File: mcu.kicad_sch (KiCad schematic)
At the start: 29 parts, among them J2 Conn_01x10, J3 Conn_01x10, J4 Conn_02x05_Odd_Even, U7 STM32F407VGTx, U8 STM809SWX6F, Y1 8MHz

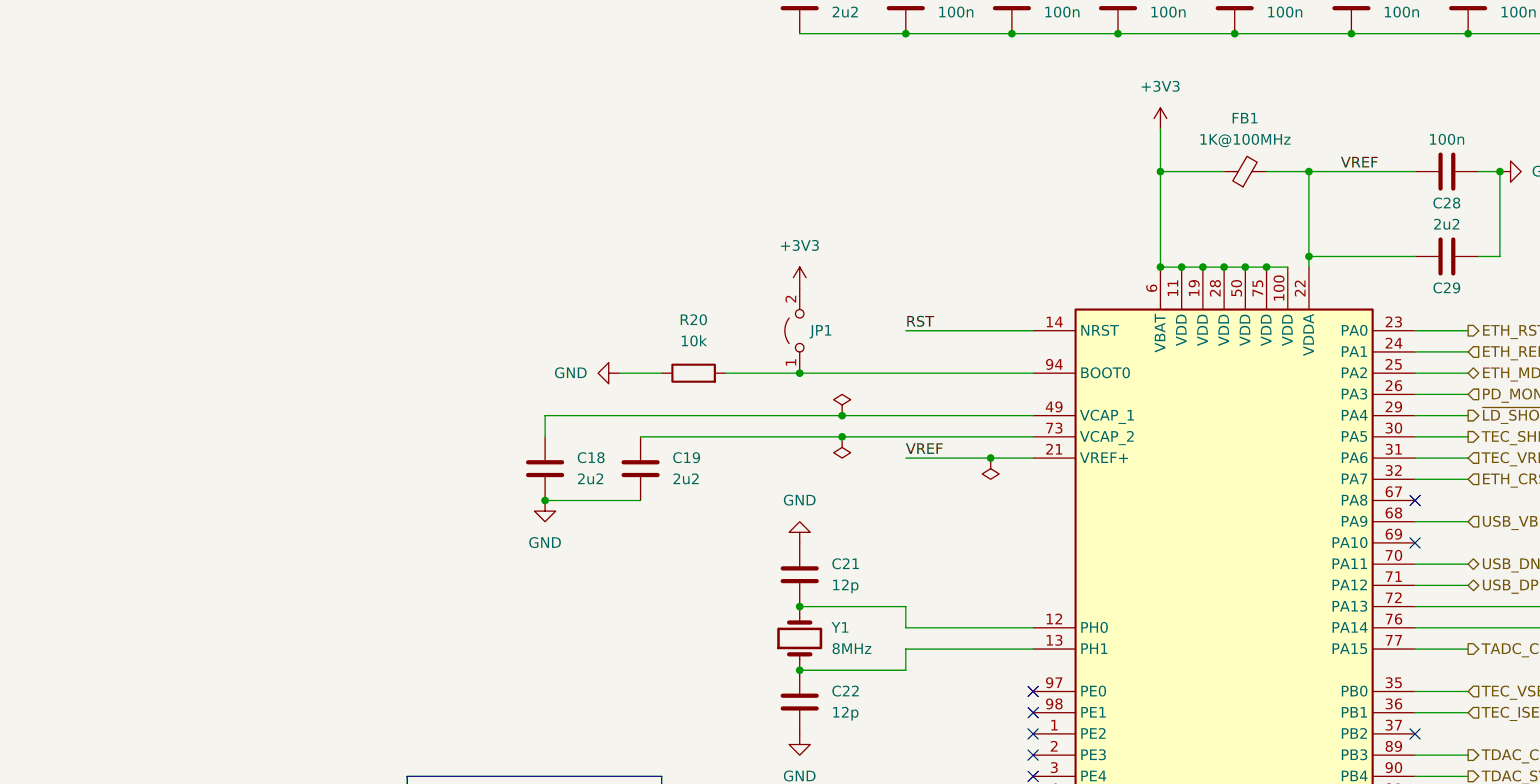
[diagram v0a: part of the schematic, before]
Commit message: sch: Add REF3033 for MCU ADC VREF
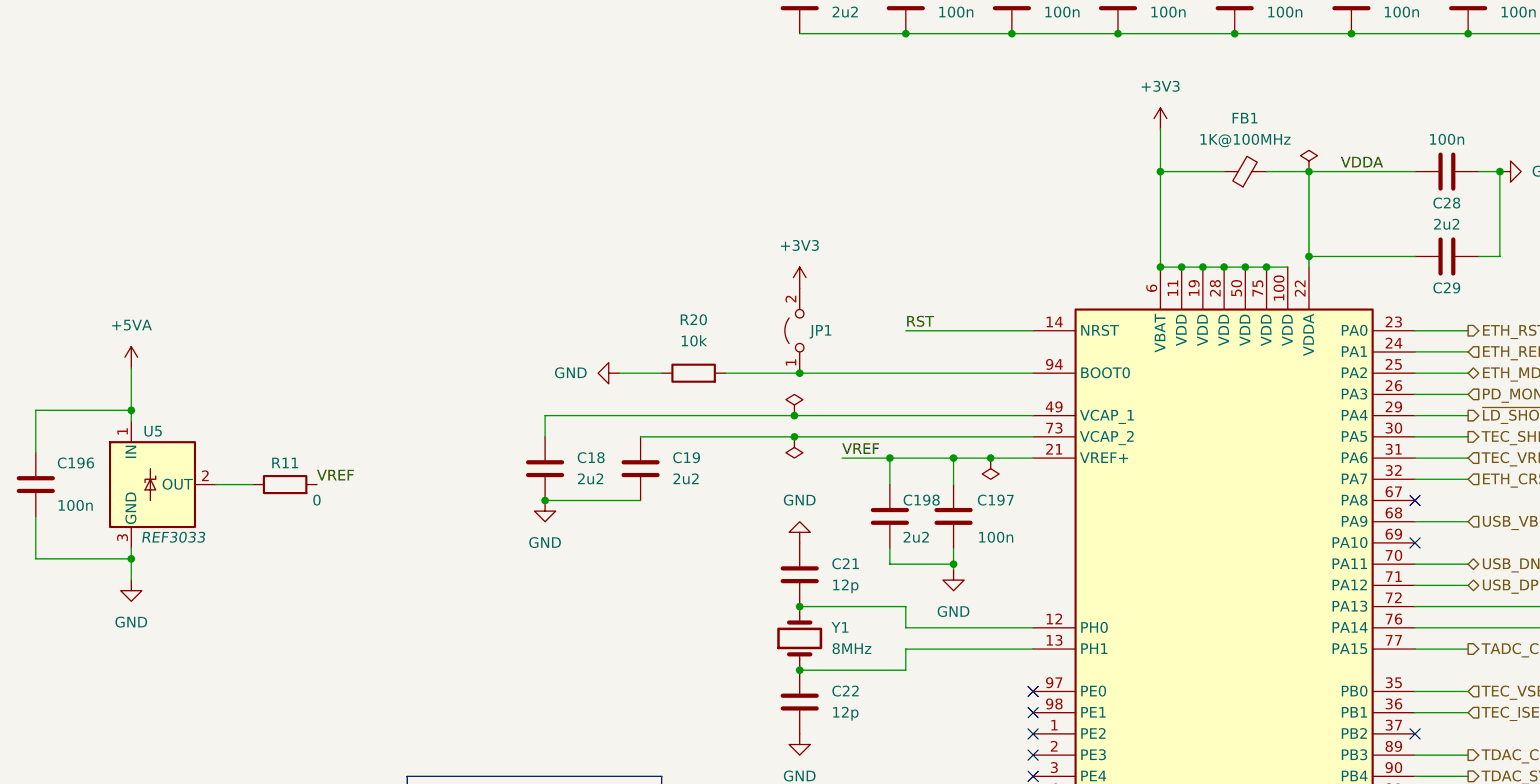
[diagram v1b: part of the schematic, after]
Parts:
- added C196, C197: 100n, Capacitor_SMD:C_0603_1608Metric, symbol Device:C
- added C198: 2u2, Capacitor_SMD:C_0603_1608Metric, symbol Device:C
- added R11: 0, Resistor_SMD:R_0603_1608Metric, symbol Device:R
- added U5: REF3033, Package_TO_SOT_SMD:SOT-23, symbol Reference_Voltage:REF3033
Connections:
- net GND: now also C196.2, C197.1, C198.1, U5.3 (GND)
- net VREF: now also C197.2, C198.2, R11.2; no longer C28.1, C29.1, FB1.2, U7.22 (VDDA)
- new net: R11.1, U5.2 (OUT)
- new net +5VA: C196.1, U5.1 (IN)
- new net VDDA: C28.1, C29.1, FB1.2, U7.22 (VDDA)

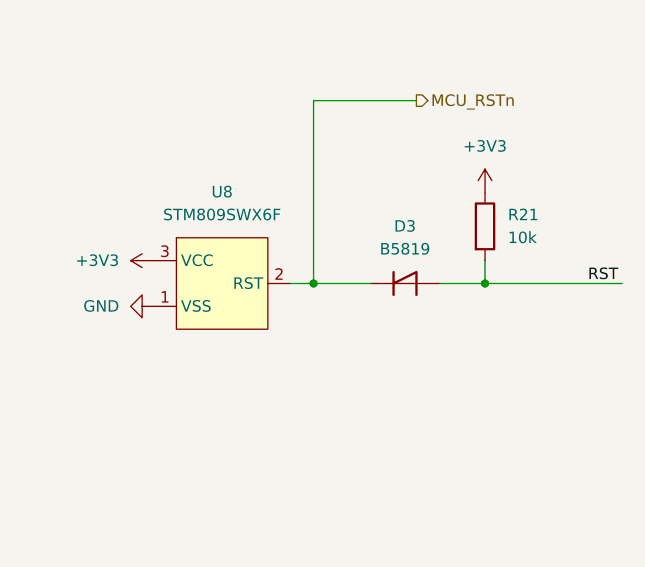
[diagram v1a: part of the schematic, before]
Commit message: sch: Do not pass MCU RST to ETH - D3 -> DNP
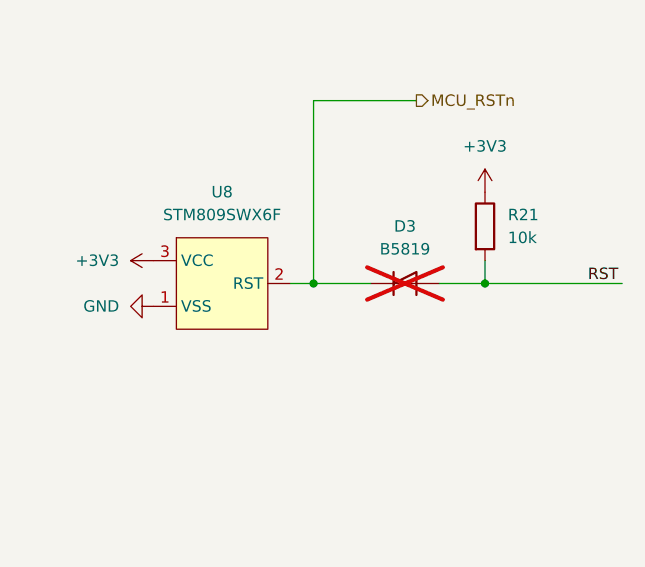
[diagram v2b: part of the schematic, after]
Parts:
- D3: now not fitted
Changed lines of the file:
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@@
   )
   (symbol (lib_id "Device:D_Shockley") (at 325.12 133.35 0) (unit 1)
-    (in_bom yes) (on_board yes) (dnp no) (fields_autoplaced)
+    (in_bom yes) (on_board yes) (dnp yes) (fields_autoplaced)
     (property "Reference" "D3" (at 325.12 127 0)
       (effects (font (size 1.27 1.27)))

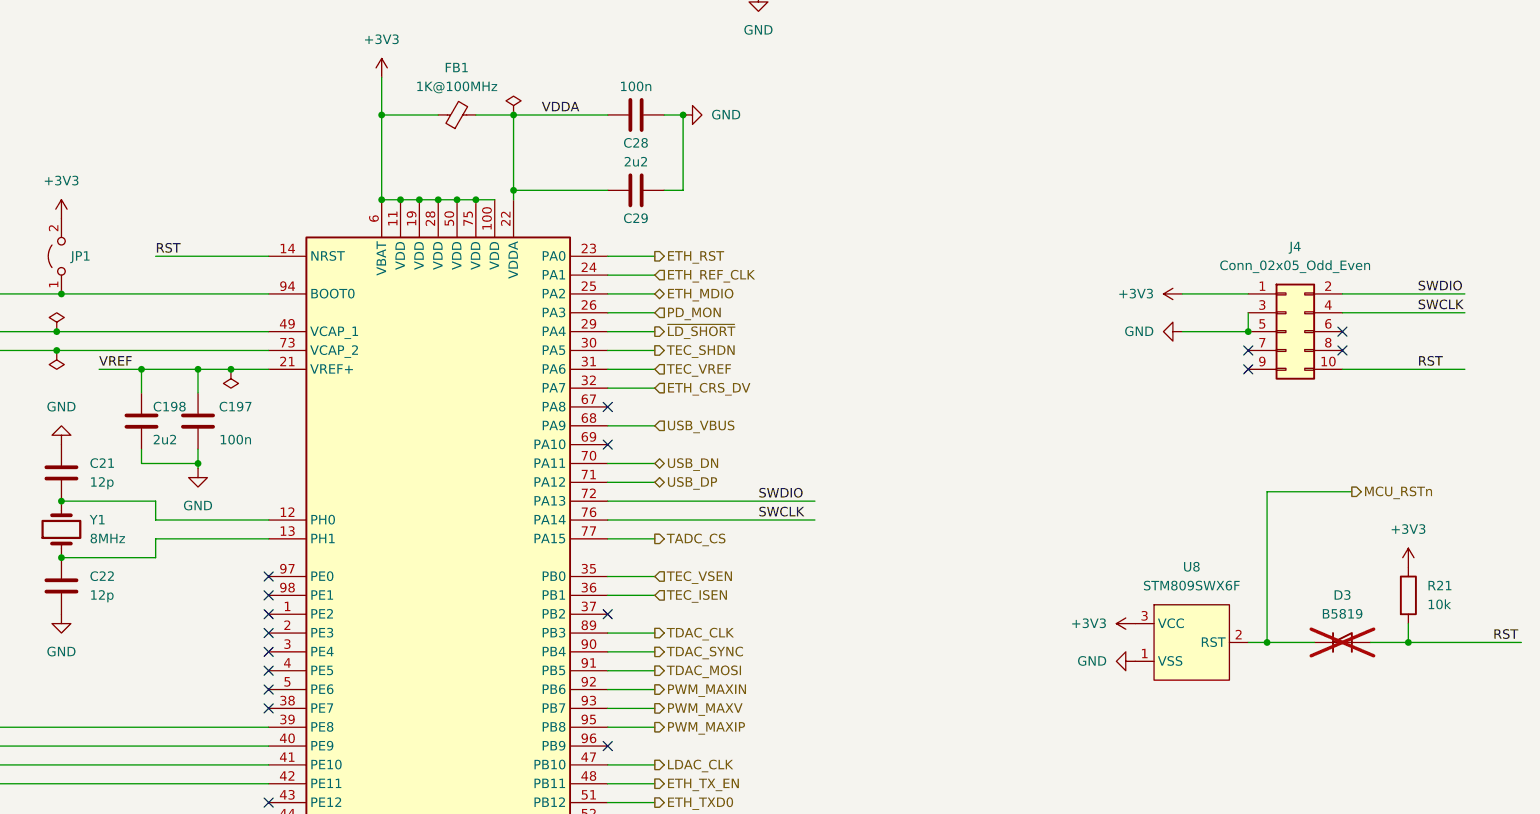
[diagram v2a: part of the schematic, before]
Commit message: sch: Change PoE RJ45 Jack and change PM1202 Symbol - Use the same PoE RJ45 as sinara-hw thermostat - Add PM1202 Power input pins (VB+, VB-) - Remove PoE softstart circuit as PM1202 has inrush current limiting - Add Pi Filter at the output of PM1202
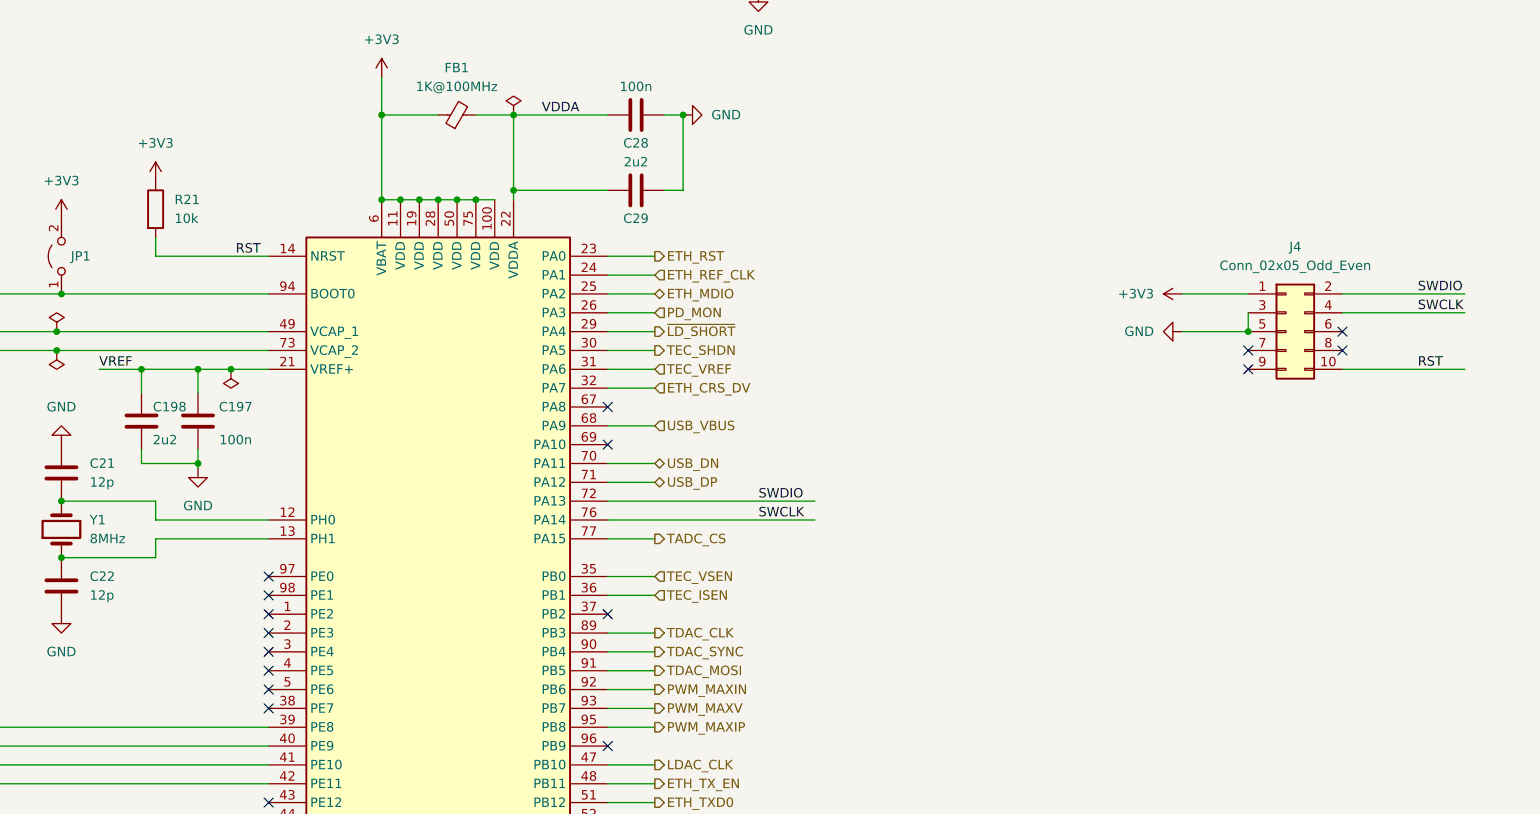
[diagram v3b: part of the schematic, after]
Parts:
- removed D3: B5819, Diode_SMD:D_SOD-323, symbol Device:D_Shockley
- removed U8: STM809SWX6F, Package_TO_SOT_SMD:SOT-23, symbol kirdy:STM809SWX6F
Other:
- moved on the sheet: R21
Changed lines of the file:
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@@
   (junction (at 232.41 45.72) (diameter 0) (color 0 0 0 0)
   )
-  (junction (at 314.96 133.35) (diameter 0) (color 0 0 0 0)
-  )
   (junction (at 200.66 213.36) (diameter 0) (color 0 0 0 0)
   )
@@
   )
   (junction (at 232.41 38.1) (diameter 0) (color 0 0 0 0)
-  )
-  (junction (at 334.01 133.35) (diameter 0) (color 0 0 0 0)
   )
   (junction (at 213.36 62.23) (diameter 0) (color 0 0 0 0)
@@
     (stroke (width 0) (type default))
   )
-  (wire (pts (xy 328.93 133.35) (xy 334.01 133.35))
-    (stroke (width 0) (type default))
-  )
-  (wire (pts (xy 312.42 133.35) (xy 314.96 133.35))
-    (stroke (width 0) (type default))
-  )
   (wire (pts (xy 226.06 139.7) (xy 232.41 139.7))
     (stroke (width 0) (type default))
@@
     (stroke (width 0) (type default))
   )
-  (wire (pts (xy 314.96 113.03) (xy 326.39 113.03))
-    (stroke (width 0) (type default))
-  )
   (wire (pts (xy 128.27 147.32) (xy 180.34 147.32))
     (stroke (width 0) (type default))
@@
     (stroke (width 0) (type default))
   )
-  (wire (pts (xy 334.01 133.35) (xy 334.01 130.81))
+  (wire (pts (xy 165.1 81.28) (xy 165.1 78.74))
     (stroke (width 0) (type default))
   )
@@
     (stroke (width 0) (type default))
   )
-  (wire (pts (xy 334.01 133.35) (xy 349.25 133.35))
-    (stroke (width 0) (type default))
-  )
   (wire (pts (xy 255.27 226.06) (xy 172.72 226.06))
     (stroke (width 0) (type default))
@@
     (stroke (width 0) (type default))
   )
-  (wire (pts (xy 314.96 133.35) (xy 321.31 133.35))
-    (stroke (width 0) (type default))
-  )
   (wire (pts (xy 226.06 137.16) (xy 232.41 137.16))
     (stroke (width 0) (type default))
@@
   )
   (wire (pts (xy 232.41 45.72) (xy 246.38 45.72))
-    (stroke (width 0) (type default))
-  )
-  (wire (pts (xy 314.96 133.35) (xy 314.96 113.03))
     (stroke (width 0) (type default))
   )
@@
     (effects (font (size 1.27 1.27)) (justify left bottom))
   )
-  (label "RST" (at 165.1 81.28 0) (fields_autoplaced)
-    (effects (font (size 1.27 1.27)) (justify left bottom))
-  )
   (label "SWDIO" (at 335.28 86.36 0) (fields_autoplaced)
     (effects (font (size 1.27 1.27)) (justify left bottom))
@@
     (effects (font (size 1.27 1.27)) (justify left bottom))
   )
-  (label "RST" (at 345.44 133.35 0) (fields_autoplaced)
-    (effects (font (size 1.27 1.27)) (justify left bottom))
-  )
   (label "VDDA" (at 217.17 62.23 0) (fields_autoplaced)
     (effects (font (size 1.27 1.27)) (justify left bottom))
@@
     (effects (font (size 1.27 1.27)) (justify left bottom))
   )
+  (label "RST" (at 175.895 81.28 0) (fields_autoplaced)
+    (effects (font (size 1.27 1.27)) (justify left bottom))
+  )
   (hierarchical_label "USB_DP" (shape bidirectional) (at 232.41 111.76 0) (fields_autoplaced)
     (effects (font (size 1.27 1.27)) (justify left))
@@
   )
   (hierarchical_label "POE_PWR_SRC" (shape input) (at 232.41 175.26 0) (fields_autoplaced)
-    (effects (font (size 1.27 1.27)) (justify left))
-  )
-  (hierarchical_label "MCU_RSTn" (shape output) (at 326.39 113.03 0) (fields_autoplaced)
     (effects (font (size 1.27 1.27)) (justify left))
   )
@@
     )
   )
-  (symbol (lib_id "Device:R") (at 334.01 127 0) (unit 1)
-    (in_bom yes) (on_board yes) (dnp no) (fields_autoplaced)
-    (property "Reference" "R21" (at 336.55 125.7299 0)
-      (effects (font (size 1.27 1.27)) (justify left))
-    )
-    (property "Value" "10k" (at 336.55 128.2699 0)
-      (effects (font (size 1.27 1.27)) (justify left))
-    )
-    (property "Footprint" "Resistor_SMD:R_0603_1608Metric" (at 332.232 127 90)
-      (effects (font (size 1.27 1.27)) hide)
-    )
-    (property "Datasheet" "~" (at 334.01 127 0)
-      (effects (font (size 1.27 1.27)) hide)
-    )
-    (property "MFR_PN" "RNCP0603FTD10K0" (at 334.01 127 0)
-      (effects (font (size 1.27 1.27)) hide)
-    )
-    (property "MFR_PN_ALT" "RMCF0603FT10K0" (at 334.01 127 0)
+  (symbol (lib_id "Device:R") (at 165.1 74.93 0) (unit 1)
+    (in_bom yes) (on_board yes) (dnp no) (fields_autoplaced)
+    (property "Reference" "R21" (at 167.64 73.6599 0)
+      (effects (font (size 1.27 1.27)) (justify left))
+    )
+    (property "Value" "10k" (at 167.64 76.1999 0)
+      (effects (font (size 1.27 1.27)) (justify left))
+    )
+    (property "Footprint" "Resistor_SMD:R_0603_1608Metric" (at 163.322 74.93 90)
+      (effects (font (size 1.27 1.27)) hide)
+    )
+    (property "Datasheet" "~" (at 165.1 74.93 0)
+      (effects (font (size 1.27 1.27)) hide)
+    )
+    (property "MFR_PN" "RNCP0603FTD10K0" (at 165.1 74.93 0)
+      (effects (font (size 1.27 1.27)) hide)
+    )
+    (property "MFR_PN_ALT" "RMCF0603FT10K0" (at 165.1 74.93 0)
       (effects (font (size 1.27 1.27)) hide)
     )
@@
         (path "/88da1dd8-9274-4b55-84fb-90006c9b6e8f/e9afb2cc-7f7f-4cb9-888a-0bfd71b1d070"
           (reference "C196") (unit 1)
-        )
-      )
-    )
-  )
-  (symbol (lib_id "kirdy:STM809SWX6F") (at 304.8 133.35 0) (unit 1)
-    (in_bom yes) (on_board yes) (dnp no) (fields_autoplaced)
-    (property "Reference" "U8" (at 304.8 123.19 0)
-      (effects (font (size 1.27 1.27)))
-    )
-    (property "Value" "STM809SWX6F" (at 304.8 125.73 0)
-      (effects (font (size 1.27 1.27)))
-    )
-    (property "Footprint" "Package_TO_SOT_SMD:SOT-23" (at 297.18 135.89 0)
-      (effects (font (size 1.27 1.27)) hide)
-    )
-    (property "Datasheet" "" (at 297.18 135.89 0)
-      (effects (font (size 1.27 1.27)) hide)
-    )
-    (property "MFR_PN" "STM809SWX6F" (at 304.8 133.35 0)
-      (effects (font (size 1.27 1.27)) hide)
-    )
-    (pin "1")
-    (pin "2")
-    (pin "3")
-    (instances
-      (project "kirdy"
-        (path "/88da1dd8-9274-4b55-84fb-90006c9b6e8f/e9afb2cc-7f7f-4cb9-888a-0bfd71b1d070"
-          (reference "U8") (unit 1)
         )
       )
@@
     )
   )
-  (symbol (lib_id "power:+3V3") (at 334.01 123.19 0) (unit 1)
-    (in_bom yes) (on_board yes) (dnp no) (fields_autoplaced)
-    (property "Reference" "#PWR056" (at 334.01 127 0)
-      (effects (font (size 1.27 1.27)) hide)
-    )
-    (property "Value" "+3V3" (at 334.01 118.11 0)
-      (effects (font (size 1.27 1.27)))
-    )
-    (property "Footprint" "" (at 334.01 123.19 0)
-      (effects (font (size 1.27 1.27)) hide)
-    )
-    (property "Datasheet" "" (at 334.01 123.19 0)
+  (symbol (lib_id "power:+3V3") (at 165.1 71.12 0) (unit 1)
+    (in_bom yes) (on_board yes) (dnp no) (fields_autoplaced)
+    (property "Reference" "#PWR056" (at 165.1 74.93 0)
+      (effects (font (size 1.27 1.27)) hide)
+    )
+    (property "Value" "+3V3" (at 165.1 66.04 0)
+      (effects (font (size 1.27 1.27)))
+    )
+    (property "Footprint" "" (at 165.1 71.12 0)
+      (effects (font (size 1.27 1.27)) hide)
+    )
+    (property "Datasheet" "" (at 165.1 71.12 0)
       (effects (font (size 1.27 1.27)) hide)
     )
@@
     )
   )
-  (symbol (lib_id "power:GND") (at 297.18 135.89 270) (unit 1)
-    (in_bom yes) (on_board yes) (dnp no) (fields_autoplaced)
-    (property "Reference" "#PWR053" (at 290.83 135.89 0)
-      (effects (font (size 1.27 1.27)) hide)
-    )
-    (property "Value" "GND" (at 293.37 135.8899 90)
-      (effects (font (size 1.27 1.27)) (justify right))
-    )
-    (property "Footprint" "" (at 297.18 135.89 0)
-      (effects (font (size 1.27 1.27)) hide)
-    )
-    (property "Datasheet" "" (at 297.18 135.89 0)
-      (effects (font (size 1.27 1.27)) hide)
-    )
-    (pin "1")
-    (instances
-      (project "kirdy"
-        (path "/88da1dd8-9274-4b55-84fb-90006c9b6e8f/e9afb2cc-7f7f-4cb9-888a-0bfd71b1d070"
-          (reference "#PWR053") (unit 1)
-        )
-      )
-    )
-  )
   (symbol (lib_id "Device:C") (at 229.87 62.23 90) (unit 1)
     (in_bom yes) (on_board yes) (dnp no)
@@
     )
   )
-  (symbol (lib_id "power:+3V3") (at 297.18 130.81 90) (unit 1)
-    (in_bom yes) (on_board yes) (dnp no) (fields_autoplaced)
-    (property "Reference" "#PWR052" (at 300.99 130.81 0)
-      (effects (font (size 1.27 1.27)) hide)
-    )
-    (property "Value" "+3V3" (at 293.37 130.8099 90)
-      (effects (font (size 1.27 1.27)) (justify left))
-    )
-    (property "Footprint" "" (at 297.18 130.81 0)
-      (effects (font (size 1.27 1.27)) hide)
-    )
-    (property "Datasheet" "" (at 297.18 130.81 0)
-      (effects (font (size 1.27 1.27)) hide)
-    )
-    (pin "1")
-    (instances
-      (project "kirdy"
-        (path "/88da1dd8-9274-4b55-84fb-90006c9b6e8f/e9afb2cc-7f7f-4cb9-888a-0bfd71b1d070"
-          (reference "#PWR052") (unit 1)
-        )
-      )
-    )
-  )
   (symbol (lib_id "power:GND") (at 303.53 91.44 270) (unit 1)
     (in_bom yes) (on_board yes) (dnp no) (fields_autoplaced)
@@
         )
       )
-    )
-  )
-  (symbol (lib_id "Device:D_Shockley") (at 325.12 133.35 0) (unit 1)
-    (in_bom yes) (on_board yes) (dnp yes) (fields_autoplaced)
-    (property "Reference" "D3" (at 325.12 127 0)
-      (effects (font (size 1.27 1.27)))
-    )
-    (property "Value" "B5819" (at 325.12 129.54 0)
-      (effects (font (size 1.27 1.27)))
-    )
-    (property "Footprint" "Diode_SMD:D_SOD-323" (at 325.12 133.35 0)
-      (effects (font (size 1.27 1.27)) hide)
-    )
-    (property "Datasheet" "~" (at 325.12 133.35 0)
-      (effects (font (size 1.27 1.27)) hide)
-    )
-    (property "MFR_PN" "B5819WS-TP" (at 325.12 133.35 0)
-      (effects (font (size 1.27 1.27)) hide)
-    )
-    (pin "1")
-    (pin "2")
-    (instances
-      (project "kirdy"
-        (path "/88da1dd8-9274-4b55-84fb-90006c9b6e8f/e9afb2cc-7f7f-4cb9-888a-0bfd71b1d070"
-          (reference "D3") (unit 1)
-        )
-      )
